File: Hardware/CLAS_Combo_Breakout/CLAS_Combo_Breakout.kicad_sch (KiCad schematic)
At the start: 67 parts

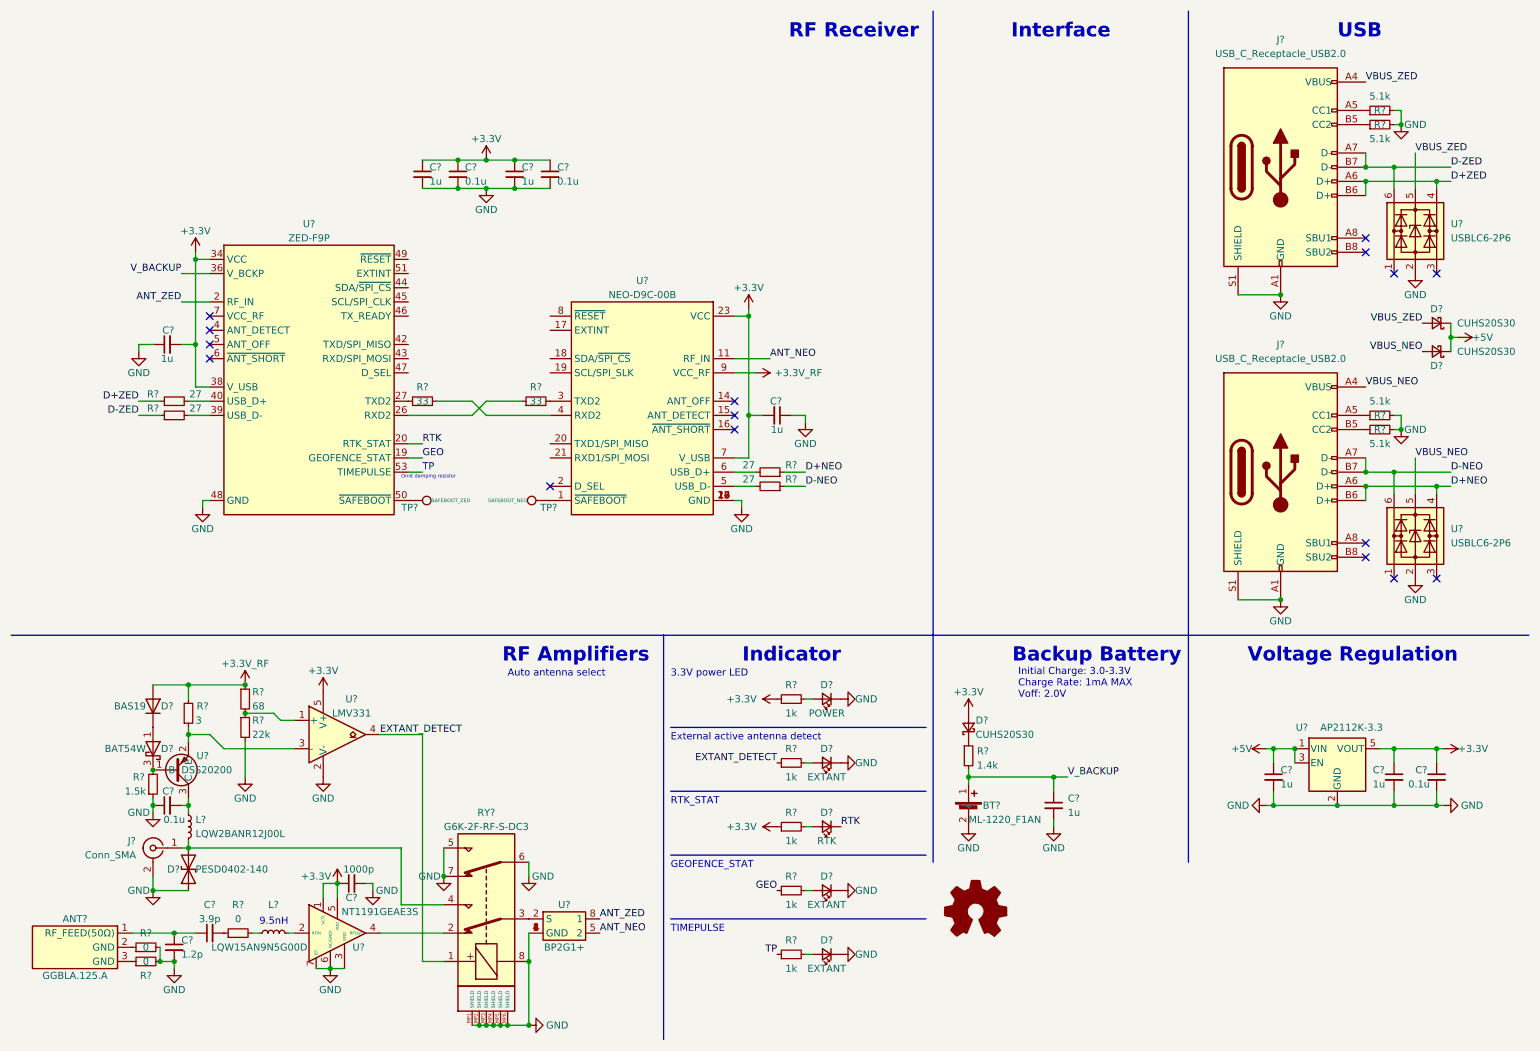
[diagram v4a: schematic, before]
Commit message: update schematic
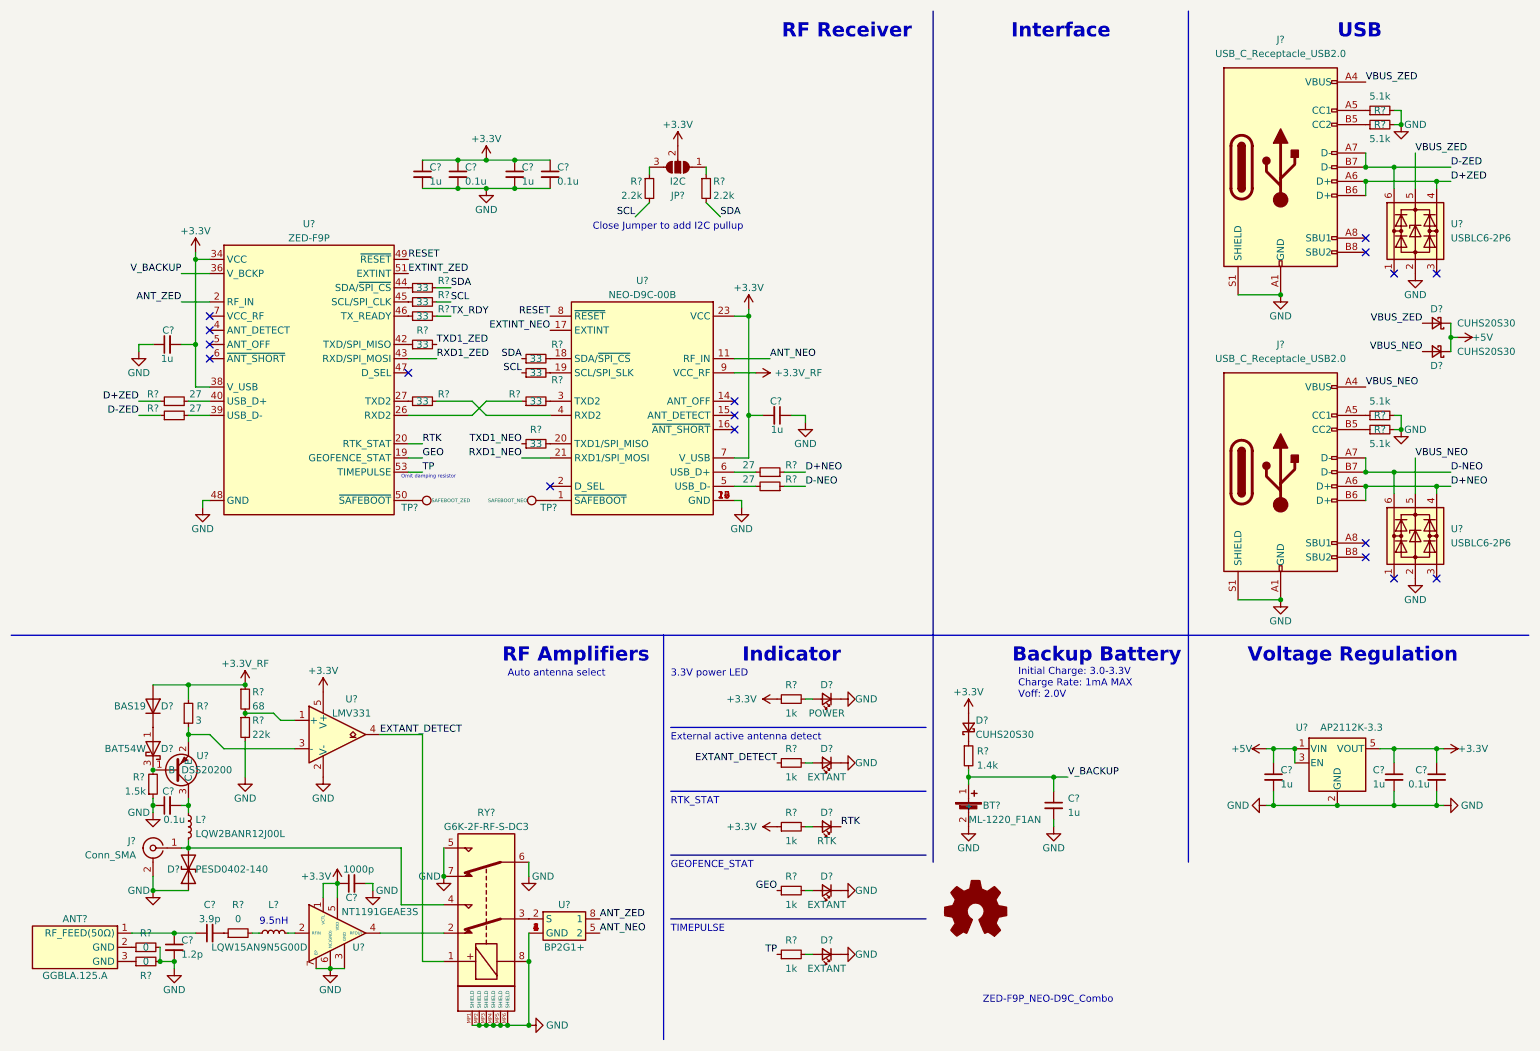
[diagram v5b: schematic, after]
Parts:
- added JP?: I2C, symbol Jumper:SolderJumper_3_Open
- added R? (x7): 33, symbol Device:R_Small
- added R? (x2): 2.2k, symbol Device:R_Small
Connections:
- net +3.3V: now also JP?.2 (C)
- net EXTINT_NEO: now reaches U?.17 (EXTINT)
- net at U?.18 (SDA/~{SPI_CS}): now also R?.2
- net at U?.19 (SCL/SPI_SLK): now also R?.2
- net at U?.20 (TXD1/SPI_MISO): now also R?.2
- net RXD1_NEO: now reaches U?.21 (RXD1/SPI_MOSI)
- net RESET: now reaches U?.8 (~{RESET})
- net RESET: now also U?.49 (~{RESET})
- net at U?.42 (TXD/SPI_MISO): now also R?.1
- net RXD1_ZED: now reaches U?.43 (RXD/SPI_MOSI)
- net at U?.44 (SDA/~{SPI_CS}): now also R?.1
- net at U?.45 (SCL/SPI_CLK): now also R?.1
- net at U?.46 (TX_READY): now also R?.1
- net EXTINT_ZED: now reaches U?.51 (EXTINT)
- new net: JP?.3 (B), R?.1
- new net: JP?.1 (A), R?.1
- new net SCL: R?.1, R?.2, R?.2
- new net SDA: R?.1, R?.2, R?.2
- new net TXD1_NEO: R?.1
- new net TXD1_ZED: R?.2
- new net TX_RDY: R?.2
- no-connect marks 16 -> 17
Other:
- note added: "Close Jumper to add I2C pullup"
- note added: "ZED-F9P_NEO-D9C_Combo"

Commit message: フットプリントの仮割り当てが完了
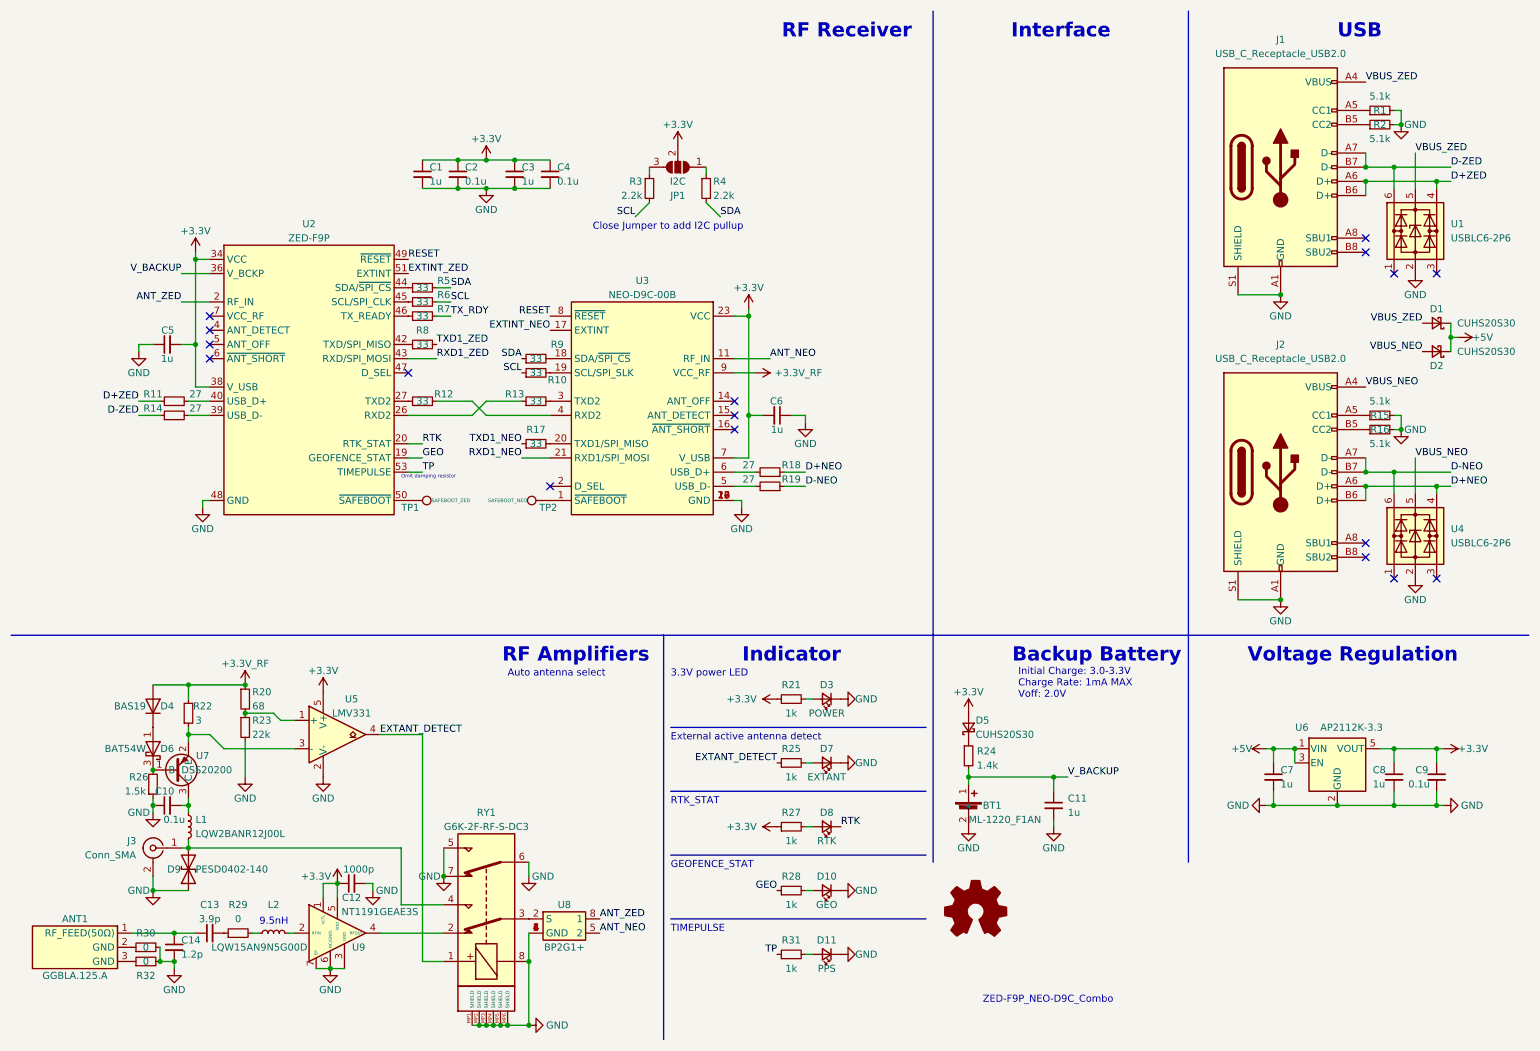
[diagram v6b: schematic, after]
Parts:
- ANT1: renamed from ANT?; footprint (none) -> GGBLA.125.A:GGBLA.125.A
- BT1: renamed from BT?; footprint ML-1220F1AN -> ML-1220_F1AN:ML-1220_F1AN
- C1, C10, C12, C13, C14, C2, C3, C4, C5, C6, C7, C8, C9: renamed from C?; footprint (none) -> Capacitor_SMD:C_0603_1608Metric
- C11: renamed from C?; footprint Capacitor_SMD:C_0603_1608Metric_Pad1.08x0.95mm_HandSolder -> Capacitor_SMD:C_0603_1608Metric
- D1, D2, D5: renamed from D?; footprint (none) -> CUHS20S30:CUHS20S30
- D10: renamed from D?; value EXTANT -> GEO; footprint (none) -> LED_SMD:LED_0603_1608Metric
- D11: renamed from D?; value EXTANT -> PPS; footprint (none) -> LED_SMD:LED_0603_1608Metric
- D3, D7, D8: renamed from D?; footprint (none) -> LED_SMD:LED_0603_1608Metric
- D6: renamed from D?; footprint Package_TO_SOT_SMD:SOT-323_SC-70 -> Package_TO_SOT_SMD:SOT-23
- D9: renamed from D?; footprint (none) -> Diode_SMD:D_0402_1005Metric
- J1, J2: renamed from J?; footprint (none) -> Connector_USB:USB_C_Receptacle_GCT_USB4085
- J3: renamed from J?; footprint (none) -> Connector_Coaxial:SMA_Samtec_SMA-J-P-X-ST-EM1_EdgeMount
- JP1: renamed from JP?; footprint (none) -> Jumper:SolderJumper-3_P1.3mm_Open_RoundedPad1.0x1.5mm_NumberLabels
- L1: renamed from L?; footprint (none) -> LQW2BANR12J00L:LQW2BANR12J00L
- L2: renamed from L?; footprint (none) -> LQW15AN9N5G00D:LQW15AN9N5G00D
- R1, R10, R11, R12, R13, R14, R15, R16, R17, R18, R19, R2, R20, R21, R22, R23, R25, R26, R27, R28, R29, R3, R30, R31, R32, R4, R5, R6, R7, R8, R9: renamed from R?; footprint (none) -> Resistor_SMD:R_0603_1608Metric
- R24: renamed from R?; footprint Resistor_SMD:R_0603_1608Metric_Pad0.98x0.95mm_HandSolder -> Resistor_SMD:R_0603_1608Metric
- RY1: renamed from RY?; footprint (none) -> G6K-2F-RF-S-DC3:G6K-2F-RF-S-DC3
- TP1, TP2: renamed from TP?; footprint (none) -> TestPoint:TestPoint_Pad_D1.0mm
- U3: renamed from U?; footprint (none) -> NEO-D9:NEO-D9
- U5: renamed from U?; footprint (none) -> Package_TO_SOT_SMD:SOT-23-5
- U7: renamed from U?; footprint (none) -> DSS20200L-7:DSS20200L-7
- U8: renamed from U?; footprint (none) -> BP2G1+:BP2G1
- U9: renamed from U?; footprint (none) -> NT1191GEAE3S:NT1191GEAE3S
- gave numbers to parts that had none: 5

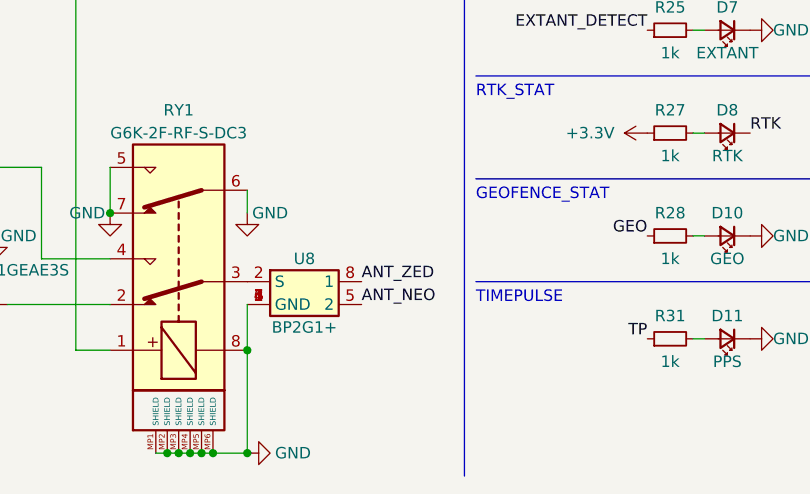
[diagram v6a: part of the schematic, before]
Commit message: 部品を配置
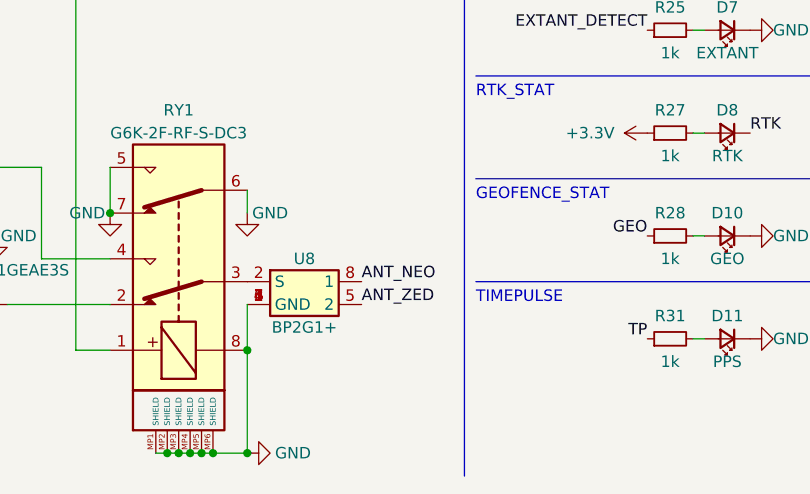
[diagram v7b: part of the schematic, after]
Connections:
- net ANT_NEO: now also U8.8 (1); no longer U8.5 (2)
- net ANT_ZED: now also U8.5 (2); no longer U8.8 (1)
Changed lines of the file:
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@@
     (effects (font (size 1.27 1.27)) (justify right bottom))
   )
-  (label "ANT_ZED" (at 118.11 175.26 0)
+  (label "ANT_ZED" (at 118.11 177.8 0)
     (effects (font (size 1.27 1.27)) (justify left bottom))
   )
@@
     (effects (font (size 1.27 1.27)) (justify left bottom))
   )
-  (label "ANT_NEO" (at 118.11 177.8 0)
+  (label "ANT_NEO" (at 118.11 175.26 0)
     (effects (font (size 1.27 1.27)) (justify left bottom))
   )

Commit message: アンテナ電源供給回路を配置
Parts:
- J3: footprint Connector_Coaxial:SMA_Samtec_SMA-J-P-X-ST-EM1_EdgeMount -> Connector_Coaxial:U.FL_Hirose_U.FL-R-SMT-1_Vertical
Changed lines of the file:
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@@
     (property "Reference" "J3" (id 0) (at 34.29 161.29 0))
     (property "Value" "Conn_SMA" (id 1) (at 30.48 163.83 0))
-    (property "Footprint" "Connector_Coaxial:SMA_Samtec_SMA-J-P-X-ST-EM1_EdgeMount" (id 2) (at 38.1 162.56 0)
+    (property "Footprint" "Connector_Coaxial:U.FL_Hirose_U.FL-R-SMT-1_Vertical" (id 2) (at 38.1 162.56 0)
       (effects (font (size 1.27 1.27)) hide)
     )
@@
     )
     (path "/c1f8d42f-0e23-4789-b87b-a02b45b47937"
-      (reference "J3") (unit 1) (value "Conn_SMA") (footprint "Connector_Coaxial:SMA_Samtec_SMA-J-P-X-ST-EM1_EdgeMount")
+      (reference "J3") (unit 1) (value "Conn_SMA") (footprint "Connector_Coaxial:U.FL_Hirose_U.FL-R-SMT-1_Vertical")
     )
     (path "/b54126b3-7985-4549-85a9-fc253ef56032"
